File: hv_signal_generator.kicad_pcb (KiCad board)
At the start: 2 copper layers, 83.8 x 121.9 mm, 210 parts, among them IC1 ATMEG328PU, J1 CONN_4, J2 CONN_10, J3 CONN_2, J4 CONN_2, J5 CONN_40, P1 CONN_6, P2 CONN_6, SW1 DPST, U1 74HC595A, U2 74HC595A, U3 74HC595A, U4 74HC595A, U5 74HC595A, U6 7400, X1 16MHz

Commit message: Complete layout
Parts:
- removed the 1PIN at (20.3, 133.3)
- removed the 1PIN at (96.5, 133.3)
- removed C14: 0.1uF, SM1206
- removed CH0, CH1, CH10, CH11, CH12, CH13, CH14, CH15, CH16, CH17, CH18, CH19, CH2, CH20, CH21, CH22, CH23, CH24, CH25, CH26, CH27, CH28, CH29, CH3, CH30, CH31, CH32, CH33, CH34, CH35, CH36, CH37, CH38, CH39, CH4, CH5, CH6, CH7, CH8, CH9: AQW216, 8DIPCMS
- removed DS1: +5V, LED-1206
- removed DS2: VCC, LED-1206
- removed DS3: PROG_MODE, LED-1206
- removed DS4: RST, LED-1206
- removed G***: LOGO, CC_A_SA_LOGO
- removed G***: LOGO, OSHWLOGO0.75IN
- removed J1: CONN_4, Molex_15-24-4441
- removed J3, J4: CONN_2, JACK_SMA
- removed J5: CONN_40, TFML-120-01-XXX-D-RA
- removed JP2: JUMPER, PIN_ARRAY_2X1
- removed JP3: ISP RESET, PIN_ARRAY_2X1
- removed R100, R125, R126, R127, R45: 1k, SM1206
- removed R101, R106, R107, R112, R114, R118, R120, R124, R24, R25, R30, R31, R36, R37, R42, R44, R50, R51, R56, R57, R62, R64, R68, R70, R74, R75, R80, R81, R86, R87, R92, R93, R98: 4.75k, SM1206
- removed R102, R103, R104, R105, R108, R109, R110, R111, R113, R115, R116, R117, R119, R121, R122, R123, R21, R22, R23, R26, R27, R28, R29, R32, R33, R34, R35, R38, R39, R40, R41, R46, R47, R48, R49, R52, R53, R54, R55, R58, R59, R60, R61, R63, R65, R66, R67, R69, R71, R72, R73, R76, R77, R78, R79, R82, R83, R84, R85, R88, R89, R90, R91, R94, R95, R96, R97: 375, SM1206
- removed R43: 10k, SM1206
- removed R99: 1Meg, SM1206
- removed U6: 7400, SO14E
- added D1: ES2F, Diodes_SMD:DO-214BA, F.Cu at (64.1, 64.8)
- added L1: 100uH, Inductors:self_cms_we-pd3, F.Cu at (82.5, 63.5)
- added LED1: +5V, LEDs:LED_0805, F.Cu at (92.7, 36.8)
- added LED2: +12V, LEDs:LED_0805, F.Cu at (97.2, 36.8)
- added P3: POWER, Connect:bornier3, F.Cu at (91.7, 19.3)
- added P4: VOUT, footprints:JACK_SMA, F.Cu at (21.6, 20.3)
- added P5: LIGHT, Pin_Headers:Pin_Header_Straight_1x02, F.Cu at (86.9, 40.5)
- added P6: MAGNET, Pin_Headers:Pin_Header_Straight_1x03, F.Cu at (89.1, 35.3)
- added Q1: IRF644PBF, TO_SOT_Packages_THT:TO-220_Neutral123_Vertical_LargePads, F.Cu at (71.1, 66.0)
- added Q2: P16NF06, TO_SOT_Packages_THT:TO-220_Neutral123_Vertical_LargePads, F.Cu at (94.0, 47.0)
- C1: value 0.1uF -> 10uF; footprint SM1206 -> Capacitors_Tantalum_SMD:TantalC_SizeD_EIA-7343_Reflow
- C10, C11, C12, C5, C8: footprint SM1206 -> Capacitors_SMD:C_1206
- C13, C3: footprint SM1206 -> Capacitors_SMD:C_1206; moved to F.Cu
- C2: value 33uF -> 0.1uF; footprint SM2917 -> Capacitors_SMD:C_1206; moved to F.Cu
- C4: value 33uF -> 0.1uF; footprint SM2917 -> Capacitors_SMD:C_1812
- C6: value 0.1uF -> 100uF,35V; footprint SM1206 -> Capacitors_Tantalum_SMD:TantalC_SizeE_EIA-7360_Reflow
- C7: value 0.01uF -> 4u7,250V; footprint SM1206 -> Capacitors_SMD:c_elec_8x10.5
- C9: value 0.1uF -> 100nF,250V; footprint SM1206 -> Capacitors_SMD:C_1812
- IC1: footprint DIP-28 -> Housings_DIP:DIP-28_W7.62mm_LongPads
- J2: value CONN_10 -> COMM_BUS; footprint HE10-10C -> Connect:he10-10d
- JP1: value JUMPER -> USB_PWR; footprint PIN_ARRAY_2X1 -> Pin_Headers:Pin_Header_Straight_1x02
- P1: value CONN_6 -> FTDI_USB; footprint PIN_ARRAY-6X1 -> Pin_Headers:Pin_Header_Angled_1x06; moved to F.Cu
- P2: value CONN_6 -> ISP; footprint pin_array_3x2 -> Pin_Headers:Pin_Header_Straight_2x03
- R1: value 4.75k -> 1k; footprint SM1206 -> Resistors_SMD:R_1206; moved to F.Cu
- R10: value 375 -> 4.75k; footprint SM1206 -> Resistors_SMD:R_1206
- R11: footprint SM1206 -> Resistors_SMD:R_1206
- R12: value 4.75k -> 375; footprint SM1206 -> Resistors_SMD:R_1206
- R13: value 4.75k -> 5k; footprint SM1206 -> Resistors_SMD:R_1206; moved to F.Cu
- R14: value 375 -> 5; footprint SM1206 -> Resistors_SMD:R_1206
- R15, R17: value 375 -> 50k; footprint SM1206 -> Resistors_SMD:R_1206
- R16: value 375 -> 100k; footprint SM1206 -> Resistors_SMD:R_1206
- R18: value 4.75k -> 10k; footprint SM1206 -> Resistors_ThroughHole:Resistor_Horizontal_RM25mm
- R19: value 4.75k -> 1Meg; footprint SM1206 -> Resistors_SMD:R_1206
- R2: value 375 -> 2k; footprint SM1206 -> Resistors_SMD:R_1206
- R20: value 375 -> 10k; footprint SM1206 -> Resistors_SMD:R_1206
- R3, R4: value 375 -> 5.1k; footprint SM1206 -> Resistors_SMD:R_1206
- R5: value 375 -> 50m; footprint SM1206 -> Resistors_SMD:R_2512
- R6: value 4.75k -> 2M; footprint SM1206 -> Resistors_SMD:R_1206; moved to F.Cu
- R7: value 4.75k -> 10k; footprint SM1206 -> Resistors_SMD:R_1206
- R8: value 375 -> 2M; footprint SM1206 -> Resistors_SMD:R_1206
- R9: value 375 -> 40k; footprint SM1206 -> Resistors_SMD:R_1206
- SW1: value DPST -> RESET; footprint SW_PUSH_6mm -> footprints:SW_PUSH_6mm
- U1: value 74HC595A -> HV513; footprint SO16E -> footprints:SOW-24; moved to F.Cu
- U2: value 74HC595A -> MAX1771; footprint SO16E -> Housings_SOIC:SOIC-8_3.9x4.9mm_Pitch1.27mm; moved to F.Cu
- U3: value 74HC595A -> MCP41050; footprint SO16E -> Housings_SOIC:SOIC-8_3.9x4.9mm_Pitch1.27mm; moved to F.Cu
- U4: value 74HC595A -> HV7802; footprint SO16E -> footprints:MSOP-8; moved to F.Cu
- U5: value 74HC595A -> AQW216; footprint SO16E -> SMD_Packages:DIP-8_SMD; moved to F.Cu
- X1: footprint HC-49V -> footprints:SparkFun-HC49U-V
- moved R17 88.8 mm to (31.5, 27.9), turned to 270 degrees
- moved R12 87.2 mm to (26.7, 42.5), turned to 0 degrees
- moved R11 81.6 mm to (35.5, 39.1)
- moved R4 72.0 mm to (53.8, 25.5), turned to 180 degrees
- moved R10 69.2 mm to (30.9, 42.5), turned to 0 degrees
- moved C2 65.3 mm to (86.7, 54.6), turned to 90 degrees
- moved C6 65.0 mm to (90.8, 55.2), turned to 90 degrees
- moved R1 63.7 mm to (92.7, 41.3)
- moved R18 58.3 mm to (20.3, 61.0)
- moved U1 57.9 mm to (29.9, 52.9)
- moved R5 56.3 mm to (62.7, 56.4)
- moved R13 56.1 mm to (45.9, 55.2), turned to 180 degrees
- moved R3 54.7 mm to (58.4, 25.5), turned to 180 degrees
- moved R16 46.2 mm to (42.2, 55.8)
- moved R9 43.5 mm to (50.3, 41.5), turned to 90 degrees
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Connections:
- 1PIN pad 1: (no net) -> GND (x2)
- C1 pad 1: +5V -> +12V
- C10 pad 2: N-00000116 -> Net-(C10-Pad2)
- C11 pad 2: N-00000127 -> Net-(C11-Pad2)
- C13 pad 2: VCC -> +5V
- C2 pad 1: +5V -> +12V
- C3 pad 1: N-00000115 -> Net-(C3-Pad1)
- C4 pad 1: +5V -> VOUT
- C4 pad 2: GND -> Net-(C4-Pad2)
- C5 pad 1: +5V -> Net-(C5-Pad1)
- C6 pad 1: +5V -> +12V
- C7 pad 1: +5V -> Net-(C7-Pad1)
- C8 pad 1: +5V -> GND
- C8 pad 2: GND -> +5V
- C9 pad 1: +5V -> Net-(C7-Pad1)
- IC1 pad 10: N-00000127 -> Net-(C11-Pad2)
- IC1 pad 11: D5/S_MOSI -> D5/LED
- IC1 pad 12: (no net) -> D6/BL
- IC1 pad 13: D7 -> D7/HV513_CS
- IC1 pad 14: D8/OE -> D8/S_SCK
- IC1 pad 15: D9/SRCLR -> D9/S_MOSI
- IC1 pad 16: D10/SS -> D10/MCP41050_CS
- IC1 pad 20: VCC -> +5V
- IC1 pad 21: (no net) -> Net-(IC1-Pad21)
- IC1 pad 23: (no net) -> A0/SHORT_CHK
- IC1 pad 24: (no net) -> A1/HV_FB
- IC1 pad 25: (no net) -> D3/A2/CURRENT_SENSE
- IC1 pad 26: (no net) -> A3/OUTPUT_SELECT
- IC1 pad 4: (no net) -> D2/SERVO
- IC1 pad 5: D3/S_SS -> D3/A2/CURRENT_SENSE
- IC1 pad 6: D4/S_SCK -> D4/SHDN
- IC1 pad 7: VCC -> +5V
- IC1 pad 9: N-00000116 -> Net-(C10-Pad2)
- J2 pad 10: D10/SS -> Net-(J2-Pad10)
- J2 pad 2: VCC -> +5V
- J2 pad 5: (no net) -> Net-(J2-Pad5)
- J2 pad 6: (no net) -> Net-(J2-Pad6)
- JP1 pad 1: VCC -> +5V
- P1 pad 1: GND -> Net-(C3-Pad1)
- P1 pad 2: (no net) -> RX
- P1 pad 3: +5V_USB -> TX
- P1 pad 4: TX -> +5V_USB
- P1 pad 5: RX -> Net-(P1-Pad5)
- P1 pad 6: N-00000115 -> GND
- P2 pad 1: D12/MISO -> GND
- P2 pad 2: VCC -> RST
- P2 pad 3: D13/SCK -> D11/MOSI
- P2 pad 4: D11/MOSI -> D13/SCK
- P2 pad 5: RST -> +5V
- P2 pad 6: GND -> D12/MISO
- R1 pad 2: OUT3 -> Net-(LED1-Pad2)
- R10 pad 1: GND -> +5V
- R10 pad 2: N-00000187 -> A3/OUTPUT_SELECT
- R11 pad 2: N-00000195 -> Net-(R11-Pad2)
- R12 pad 1: +5V -> Net-(R12-Pad1)
- R12 pad 2: OUT0 -> +5V
- R13 pad 1: +5V -> Net-(C7-Pad1)
- R13 pad 2: OUT11 -> Net-(R13-Pad2)
- R14 pad 1: N-00000184 -> HV
- R14 pad 2: +5V -> Net-(C7-Pad1)
- R15 pad 1: N-00000183 -> GND
- R15 pad 2: +5V -> D3/A2/CURRENT_SENSE
- R16 pad 1: N-00000174 -> Net-(R16-Pad1)
- R16 pad 2: +5V -> HV
- R17 pad 1: N-00000207 -> +5V
- R17 pad 2: +5V -> A0/SHORT_CHK
- R18 pad 1: +5V -> GND
- R18 pad 2: OUT13 -> VOUT
- R19 pad 1: +5V -> Net-(C10-Pad2)
- R19 pad 2: OUT14 -> Net-(C11-Pad2)
- R2 pad 1: N-00000171 -> +12V
- R2 pad 2: +5V -> Net-(LED2-Pad2)
- R20 pad 1: GND -> RST
- R20 pad 2: N-00000180 -> +5V
- R3 pad 1: N-00000173 -> +5V
- R3 pad 2: +5V -> A4/SDA
- R4 pad 1: N-00000189 -> +5V
- R4 pad 2: +5V -> A5/SCL
- R5 pad 1: N-00000194 -> Net-(Q1-Pad3)
- R5 pad 2: +5V -> GND
- R6 pad 1: +5V -> Net-(C7-Pad1)
- R6 pad 2: OUT5 -> Net-(R6-Pad2)
- R7 pad 1: +5V -> Net-(R7-Pad1)
- R7 pad 2: OUT6 -> GND
- R8 pad 1: GND -> A1/HV_FB
- R8 pad 2: N-00000191 -> Net-(C7-Pad1)
- R9 pad 2: N-00000188 -> A1/HV_FB
- U1 pad 1: OUT1 -> (no net)
- U1 pad 10: D9/SRCLR -> D9/S_MOSI
- U1 pad 11: D4/S_SCK -> GND
- U1 pad 12: D3/S_SS -> (no net)
- U1 pad 13: D8/OE -> GND
- U1 pad 14: D5/S_MOSI -> GND
- U1 pad 15: OUT0 -> Net-(C4-Pad2)
- U1 pad 16: +5V -> Net-(C4-Pad2)
- U1 pad 2: OUT2 -> +5V
- U1 pad 3: OUT3 -> Net-(U1-Pad3)
- U1 pad 4: OUT4 -> D6/BL
- U1 pad 5: OUT5 -> Net-(U1-Pad5)
- U1 pad 6: OUT6 -> D8/S_SCK
- U1 pad 7: OUT7 -> D7/HV513_CS
- U1 pad 8: GND -> Net-(U1-Pad8)
- U1 pad 9: N-0000038 -> Net-(U1-Pad9)
- U2 pad 1: OUT9 -> Net-(Q1-Pad1)
- U2 pad 2: OUT10 -> +12V
- U2 pad 3: OUT11 -> Net-(R6-Pad2)
- U2 pad 4: OUT12 -> D4/SHDN
- U2 pad 5: OUT13 -> Net-(C5-Pad1)
- U2 pad 6: OUT14 -> GND
- U2 pad 7: OUT15 -> GND
- U2 pad 8: GND -> Net-(Q1-Pad3)
- U3 pad 1: OUT17 -> D10/MCP41050_CS
- U3 pad 2: OUT18 -> D8/S_SCK
- U3 pad 3: OUT19 -> D9/S_MOSI
- U3 pad 4: OUT20 -> GND
- U3 pad 5: OUT21 -> Net-(R6-Pad2)
- U3 pad 6: OUT22 -> Net-(R7-Pad1)
- U3 pad 7: OUT23 -> Net-(R7-Pad1)
- U3 pad 8: GND -> +5V
- U4 pad 1: OUT25 -> Net-(C7-Pad1)
- U4 pad 2: OUT26 -> Net-(R13-Pad2)
- U4 pad 3: OUT27 -> Net-(R16-Pad1)
- U4 pad 4: OUT28 -> (no net)
- U4 pad 5: OUT29 -> (no net)
- U4 pad 6: OUT30 -> D3/A2/CURRENT_SENSE
- U4 pad 7: OUT31 -> (no net)
- U5 pad 1: OUT33 -> Net-(R12-Pad1)
- U5 pad 2: OUT34 -> A3/OUTPUT_SELECT
- U5 pad 3: OUT35 -> A3/OUTPUT_SELECT
- U5 pad 4: OUT36 -> Net-(R11-Pad2)
- U5 pad 5: OUT37 -> A0/SHORT_CHK
- U5 pad 6: OUT38 -> Net-(P4-Pad1)
- U5 pad 7: OUT39 -> Net-(P4-Pad1)
- U5 pad 8: GND -> VOUT
- X1 pad 1: N-00000127 -> Net-(C11-Pad2)
- X1 pad 2: N-00000116 -> Net-(C10-Pad2)
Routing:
- net HV: track 597.1 -> 10.9 mm, vias 45 -> 0
- net HVGND: track 569.1 -> 0.00 mm, vias 25 -> 0
- net +5V: track 712.7 -> 231.2 mm, vias 34 -> 6
- net GND: track 728.2 -> 302.4 mm, vias 40 -> 22
- net HVOUT23: track 132.6 -> 0.00 mm, vias 5 -> 0
- net VCC: track 126.4 -> 0.00 mm, vias 7 -> 0
- net HVOUT21: track 120.4 -> 0.00 mm, vias 5 -> 0
- net HVOUT15: track 116.8 -> 0.00 mm, vias 5 -> 0
- net HVOUT39: track 108.9 -> 0.00 mm, vias 3 -> 0
- net HVOUT7: track 106.6 -> 0.00 mm, vias 4 -> 0
- net HVOUT31: track 106.5 -> 0.00 mm, vias 4 -> 0
- net HVOUT38: track 106.4 -> 0.00 mm, vias 4 -> 0
- net HVOUT19: track 97.5 -> 0.00 mm, vias 5 -> 0
- net HVOUT30: track 97.1 -> 0.00 mm, vias 4 -> 0
- net HVOUT29: track 95.3 -> 0.00 mm, vias 2 -> 0
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- added copper zone on F.Cu, net +12V
- added copper zone on F.Cu, net Net-(C7-Pad1)
- added copper zone on F.Cu, net Net-(D1-Pad2)
- added copper zone on F.Cu, net Net-(Q1-Pad1)
- added copper zone on F.Cu, net Net-(Q1-Pad3)
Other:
- board size 83.8 x 121.9 mm -> 83.8 x 56.1 mm
- net class Default: clearance 0.2032 -> 0.4; trace_width 0.2032 -> 0.254; via_dia 0.635 -> 1.2; via_drill 0.381 -> 0.8
- net class HV removed
- rule trace_clearance: 0.2032 -> 0.4
- board text added: "+12V"
- board text added: "HV signal generator board v0.1"
- board text removed: "+"
- board text removed: "1"
- board text removed: "40-channel HV Switching Board v2.1 http://microfluidics.utoronto.ca/dropbot"
- board text removed: "ISP"
- board text removed: "ISP RESET"
- board text removed: "Licensed under a Creative Commons Attribution-ShareAlike 3.0 Unported License"
- board text removed: "PROG MODE"
- board text removed: "RST"
- board text removed: "USB PWR"
- board text removed: "VCC"
- board text removed: "VCC-5V"

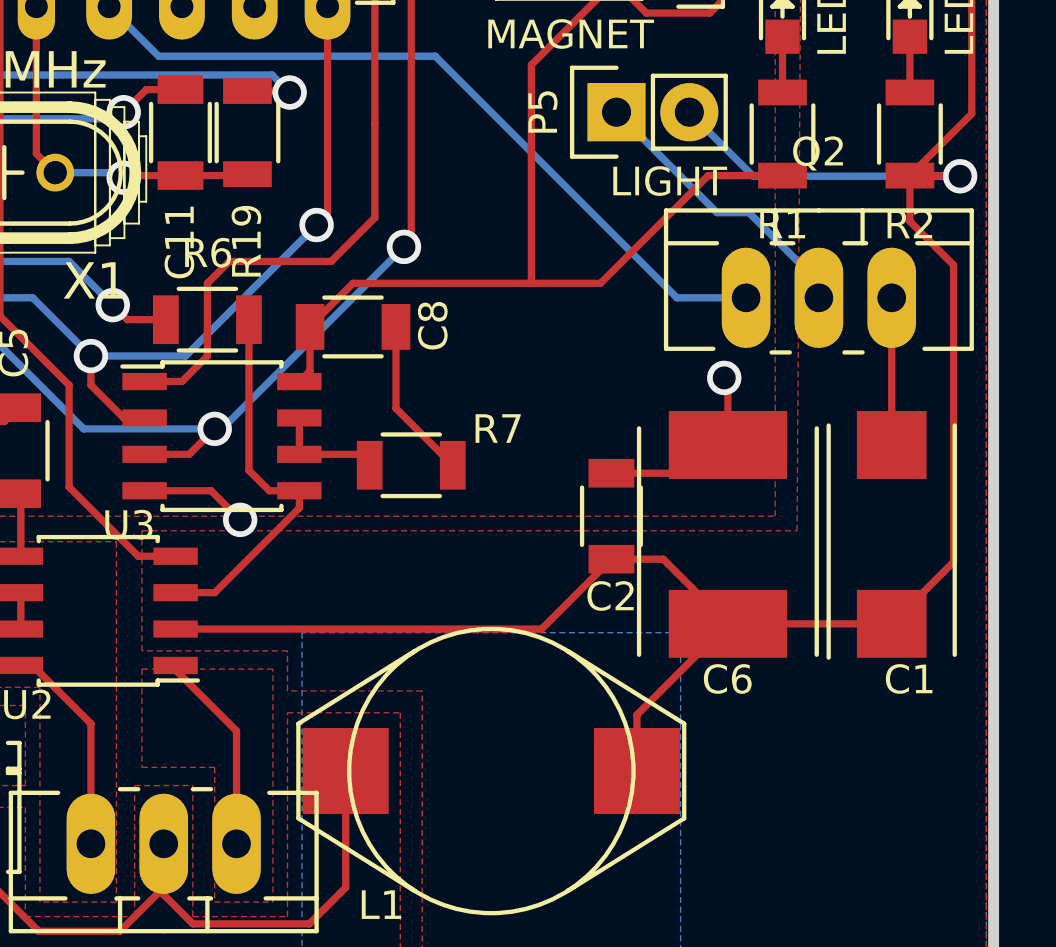
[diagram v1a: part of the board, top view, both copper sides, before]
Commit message: Move C1 and C2 closer to MAX1771 chip and ...
Add layout notes
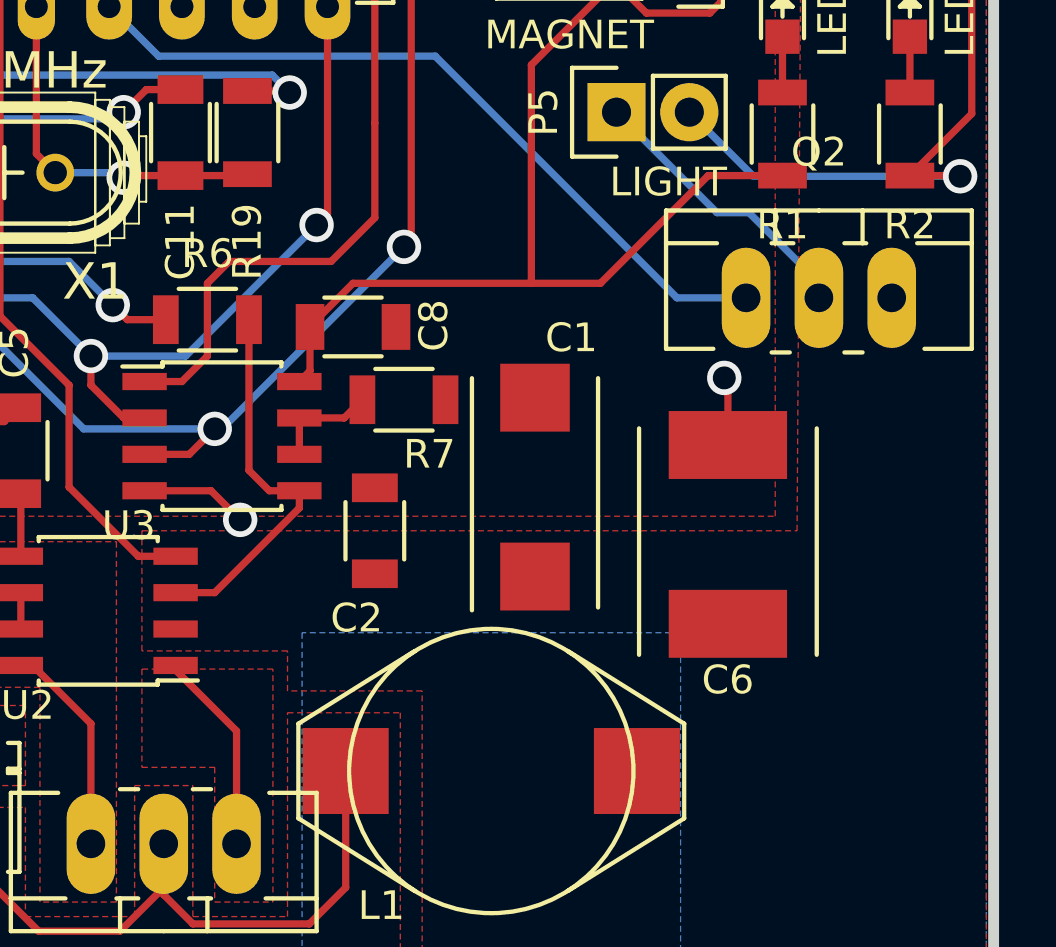
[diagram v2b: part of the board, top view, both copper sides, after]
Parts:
- moved C1 12.6 mm to (84.1, 53.6)
- moved C2 8.27 mm to (78.5, 55.1)
- moved R7 2.30 mm to (79.5, 50.5)
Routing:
- net +12V: track 88.8 -> 37.5 mm
- net GND: track 302.4 -> 287.7 mm
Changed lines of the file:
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@@
     (thickness 1.6002)
     (drawings 9)
-    (tracks 636)
+    (tracks 618)
     (zones 0)
     (modules 57)
@@
     (pad_to_mask_clearance 0.254)
     (aux_axis_origin 0 0)
-    (grid_origin 60.452 55.118)
+    (grid_origin 66.929 14.605)
     (visible_elements 7FFFFFFF)
     (pcbplotparams
@@
   )
   (module Capacitors_Tantalum_SMD:TantalC_SizeD_EIA-7343_Reflow (layer Front)
-    (at 96.52 55.245 90)
+    (at 84.074 53.594 90)
     (descr "Tantal Cap. , Size D, EIA-7343, Reflow")
     (tags "Tantal Capacitor Size-D EIA-7343 Reflow")
     (attr smd)
-    (fp_text reference C1 (at -5.08 0.635 180) (layer F.SilkS)
+    (fp_text reference C1 (at 5.207 1.27 180) (layer F.SilkS)
       (effects (font (size 1 1) (thickness 0.15)))
     )
@@
   )
   (module Resistors_SMD:R_1206 (layer Front)
-    (at 79.756 52.832)
+    (at 79.502 50.546)
     (descr "Resistor SMD 1206, reflow soldering, Vishay (see dcrcw.pdf)")
     (tags "resistor 1206")
     (attr smd)
-    (fp_text reference R7 (at 3.0226 -1.2446 180) (layer F.SilkS)
+    (fp_text reference R7 (at 0.889 1.905 180) (layer F.SilkS)
       (effects (font (size 1 1) (thickness 0.15)))
     )
@@
   )
   (module Capacitors_SMD:C_1206 (layer Front)
-    (at 86.741 54.61 90)
+    (at 78.486 55.118 90)
     (descr "Capacitor SMD 1206, reflow soldering, AVX (see smccp.pdf)")
     (tags "capacitor 1206")
     (attr smd)
-    (fp_text reference C2 (at -2.8194 0 180) (layer F.SilkS)
+    (fp_text reference C2 (at -3.048 -0.635 180) (layer F.SilkS)
       (effects (font (size 1 1) (thickness 0.15)))
     )
@@
   (via (at 73.787 54.737) (size 1.2) (drill 0.8) (layers Front Back) (net 1))
   (segment (start 72.771 53.721) (end 73.787 54.737) (width 0.254) (layer Front) (net 1))
-  (segment (start 79.224 48.006) (end 79.224 50.85) (width 0.254) (layer Front) (net 1))
-  (segment (start 79.224 50.85) (end 81.206 52.832) (width 0.254) (layer Front) (net 1))
   (segment (start 64.262 51.308) (end 65.556 51.308) (width 0.254) (layer Front) (net 1))
   (via (at 64.262 51.308) (size 1.2) (drill 0.8) (layers Front Back) (net 1))
@@
   (segment (start 47.0684 64.5414) (end 47.0684 62.519) (width 0.254) (layer Front) (net 1) (status 10))
   (segment (start 47.0684 62.519) (end 46.5934 62.044) (width 0.254) (layer Front) (net 1) (status 20))
-  (segment (start 86.4616 53.0084) (end 86.36 53.11) (width 0.254) (layer Front) (net 1) (status 30))
-  (segment (start 86.5632 52.9068) (end 86.36 53.11) (width 0.254) (layer Front) (net 1) (status 30))
   (segment (start 35.4584 37.6406) (end 35.4584 32.58058) (width 0.254) (layer Front) (net 1) (status 30))
   (segment (start 35.4584 32.58058) (end 35.34156 32.46374) (width 0.254) (layer Front) (net 1) (status 30))
@@
   (segment (start 97.155 35.78098) (end 97.155 31.115) (width 0.254) (layer Front) (net 1) (status 30))
   (segment (start 97.155 31.115) (end 96.52 30.48) (width 0.254) (layer Front) (net 1) (status 30))
-  (segment (start 86.36 53.11) (end 89.82 53.11) (width 0.254) (layer Front) (net 1) (status 30))
   (segment (start 89.82 53.11) (end 90.805 52.125) (width 0.254) (layer Front) (net 1) (status 30))
-  (segment (start 96.52 46.99) (end 96.52 52.125) (width 0.254) (layer Front) (net 1) (status 30))
   (segment (start 92.48902 35.56) (end 92.71 35.78098) (width 0.254) (layer Front) (net 1) (status 30))
   (segment (start 86.5378 35.2806) (end 86.5378 36.2712) (width 0.254) (layer Front) (net 2))
@@
   (segment (start 66.134 56.007) (end 66.134 53.918) (width 0.254) (layer Front) (net 6))
   (segment (start 66.134 53.918) (end 66.04 53.824) (width 0.254) (layer Front) (net 6))
-  (segment (start 71.534 58.547) (end 84.304 58.547) (width 0.254) (layer Front) (net 7))
-  (segment (start 84.304 58.547) (end 86.741 56.11) (width 0.254) (layer Front) (net 7))
   (segment (start 98.9076 42.7482) (end 91.694 42.7482) (width 0.254) (layer Back) (net 7))
   (segment (start 91.694 42.7482) (end 89.4588 40.513) (width 0.254) (layer Back) (net 7) (status 20))
@@
   (segment (start 99.314 27.178) (end 99.314 40.566) (width 0.254) (layer Front) (net 7))
   (segment (start 96.774 24.638) (end 99.314 27.178) (width 0.254) (layer Front) (net 7))
-  (segment (start 86.13 55.88) (end 86.36 56.11) (width 0.254) (layer Front) (net 7) (status 30))
-  (segment (start 86.36 56.11) (end 88.55 56.11) (width 0.254) (layer Front) (net 7) (status 10))
-  (segment (start 88.55 56.11) (end 90.805 58.365) (width 0.254) (layer Front) (net 7) (status 20))
-  (segment (start 87.63 63.5) (end 87.63 61.54) (width 0.254) (layer Front) (net 7) (status 10))
-  (segment (start 87.63 61.54) (end 90.805 58.365) (width 0.254) (layer Front) (net 7) (status 20))
-  (segment (start 90.805 58.365) (end 96.52 58.365) (width 0.254) (layer Front) (net 7) (status 30))
-  (segment (start 97.155 42.725) (end 97.155 44.323) (width 0.254) (layer Front) (net 7) (status 10))
-  (segment (start 98.679 56.206) (end 96.52 58.365) (width 0.254) (layer Front) (net 7) (status 20))
-  (segment (start 98.679 45.847) (end 98.679 56.206) (width 0.254) (layer Front) (net 7))
-  (segment (start 97.155 44.323) (end 98.679 45.847) (width 0.254) (layer Front) (net 7))
   (segment (start 71.194 47.752) (end 69.85 47.752) (width 0.254) (layer Front) (net 8))
   (segment (start 58.18 45.96) (end 58.18 56.388) (width 0.254) (layer Front) (net 8))
@@
   (segment (start 63.067 59.817) (end 62.738 59.488) (width 0.254) (layer Front) (net 39))
   (segment (start 68.453 65.913) (end 68.58 66.04) (width 0.254) (layer Front) (net 39))
+  (segment (start 75.852 51.181) (end 77.417 51.181) (width 0.254) (layer Front) (net 40))
+  (segment (start 77.417 51.181) (end 78.052 50.546) (width 0.254) (layer Front) (net 40))
   (segment (start 75.852 52.451) (end 75.852 51.181) (width 0.254) (layer Front) (net 40))
-  (segment (start 75.852 52.451) (end 77.925 52.451) (width 0.254) (layer Front) (net 40))
-  (segment (start 77.925 52.451) (end 78.306 52.832) (width 0.254) (layer Front) (net 40))
   (segment (start 32.766 39.878) (end 34.7958 39.878) (width 0.254) (layer Front) (net 41) (status 10))
   (segment (start 34.7958 39.878) (end 35.4584 40.5406) (width 0.254) (layer Front) (net 41) (status 20))
